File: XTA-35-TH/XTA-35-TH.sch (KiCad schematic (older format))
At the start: 28 parts, among them J1 XTA_Connector, J2 XTA Power, J3 LED, J4 SD0, J5 SD1, J6 DEBUG, SW1 Boot Override, SW2 Reset, U1 74LVC245, U2 74LVC245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

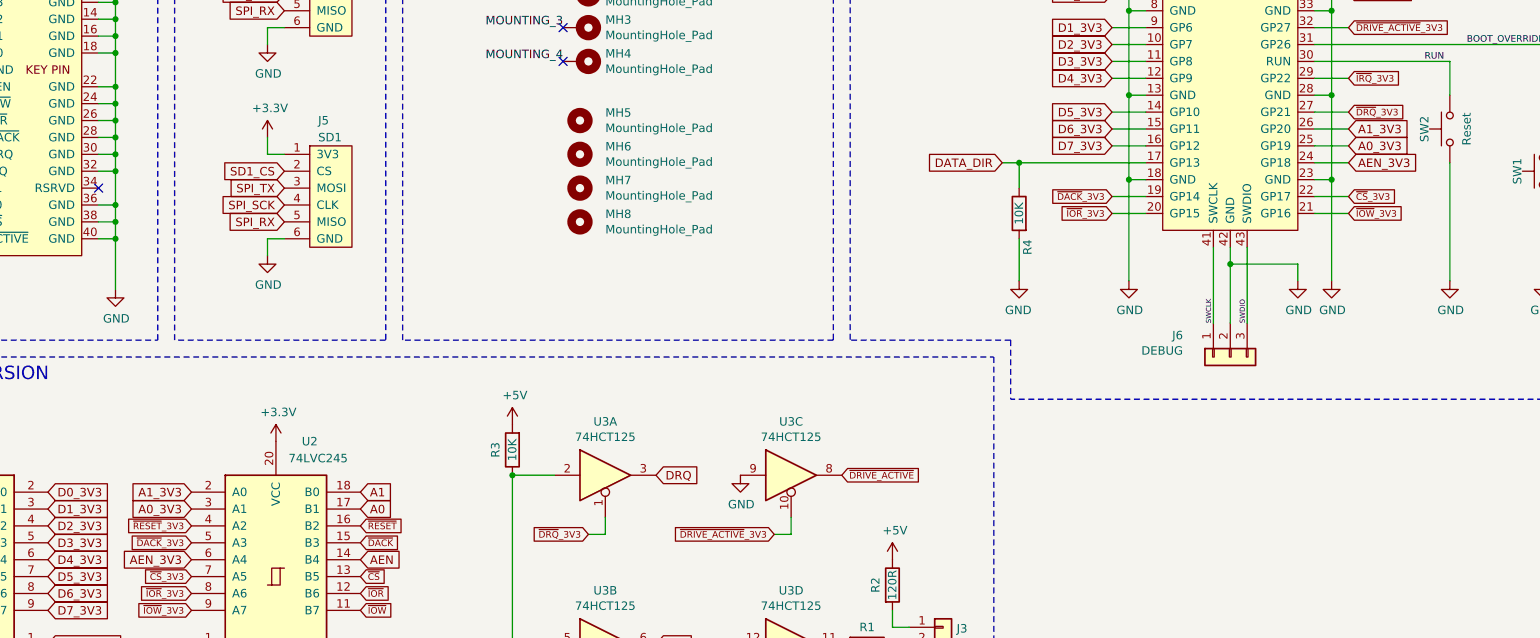
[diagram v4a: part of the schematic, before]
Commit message: Swap A0/A1 pin assignments.
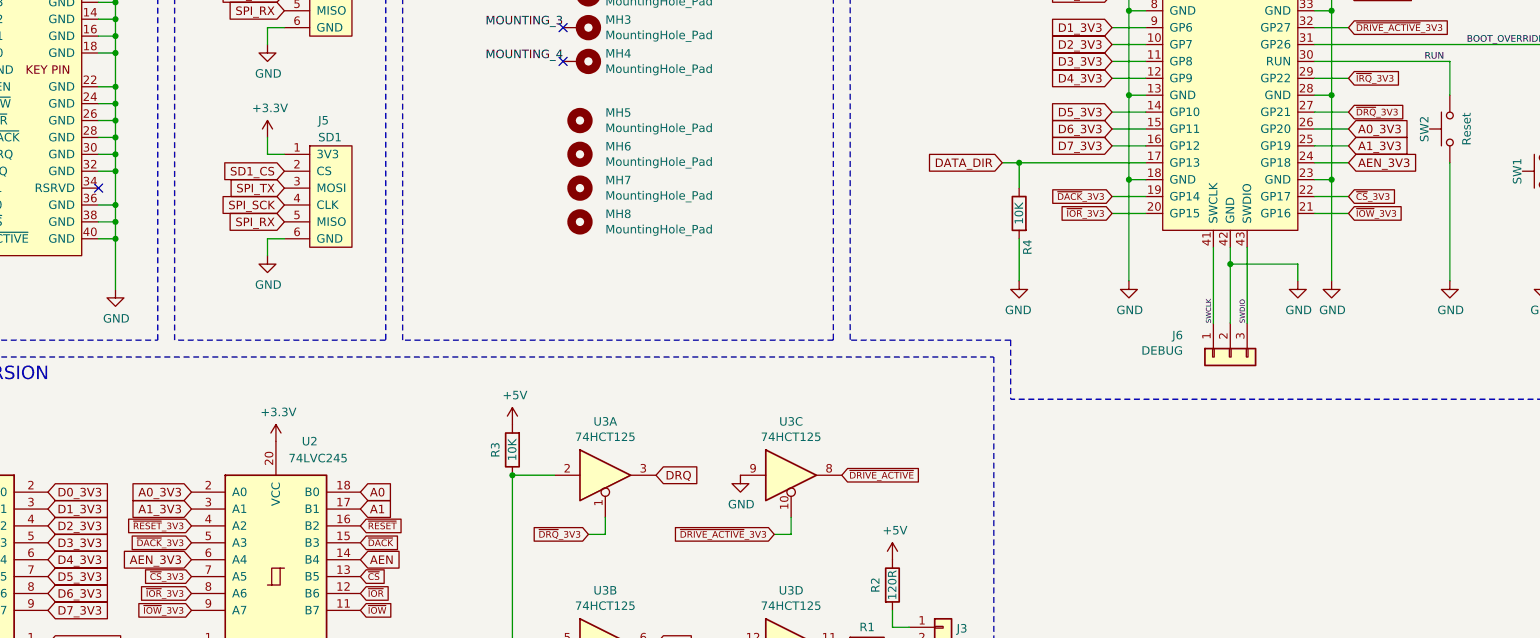
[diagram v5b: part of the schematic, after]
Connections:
- net A0: now also U2.18 (B0); no longer U2.17 (B1)
- net A0_3V3: now also U2.2 (A0), U5.26 (GP20); no longer U2.3 (A1), U5.25 (GP19)
- net A1: now also U2.17 (B1); no longer U2.18 (B0)
- net A1_3V3: now also U2.3 (A1), U5.25 (GP19); no longer U2.2 (A0), U5.26 (GP20)
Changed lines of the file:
@@
 Text GLabel 8150 2450 0    50   Input ~ 0
 D7_3V3
+Text GLabel 9550 2350 2    50   Input ~ 0
+A0_3V3
+Wire Wire Line
+	8150 1950 8350 1950
 Text GLabel 9550 2450 2    50   Input ~ 0
-A0_3V3
-Wire Wire Line
-	8150 1950 8350 1950
-Text GLabel 9550 2350 2    50   Input ~ 0
 A1_3V3
 Wire Wire Line
@@
 Text Label 9350 1250 0    39   ~ 0
 3V3_EN
+Text GLabel 2700 4600 0    50   Input ~ 0
+A1_3V3
 Text GLabel 2700 4500 0    50   Input ~ 0
-A1_3V3
-Text GLabel 2700 4600 0    50   Input ~ 0
 A0_3V3
 Text GLabel 2700 4800 0    39   Input ~ 0
@@
 Text GLabel 2700 4900 0    50   Input ~ 0
 AEN_3V3
-Text GLabel 3700 4500 2    50   Input ~ 0
+Text GLabel 3700 4600 2    50   Input ~ 0
 A1
 Text GLabel 3700 4900 2    50   Input ~ 0
@@
 Wire Wire Line
 	7850 950  8350 950
-Text GLabel 3700 4600 2    50   Input ~ 0
+Text GLabel 3700 4500 2    50   Input ~ 0
 A0
 Wire Wire Line

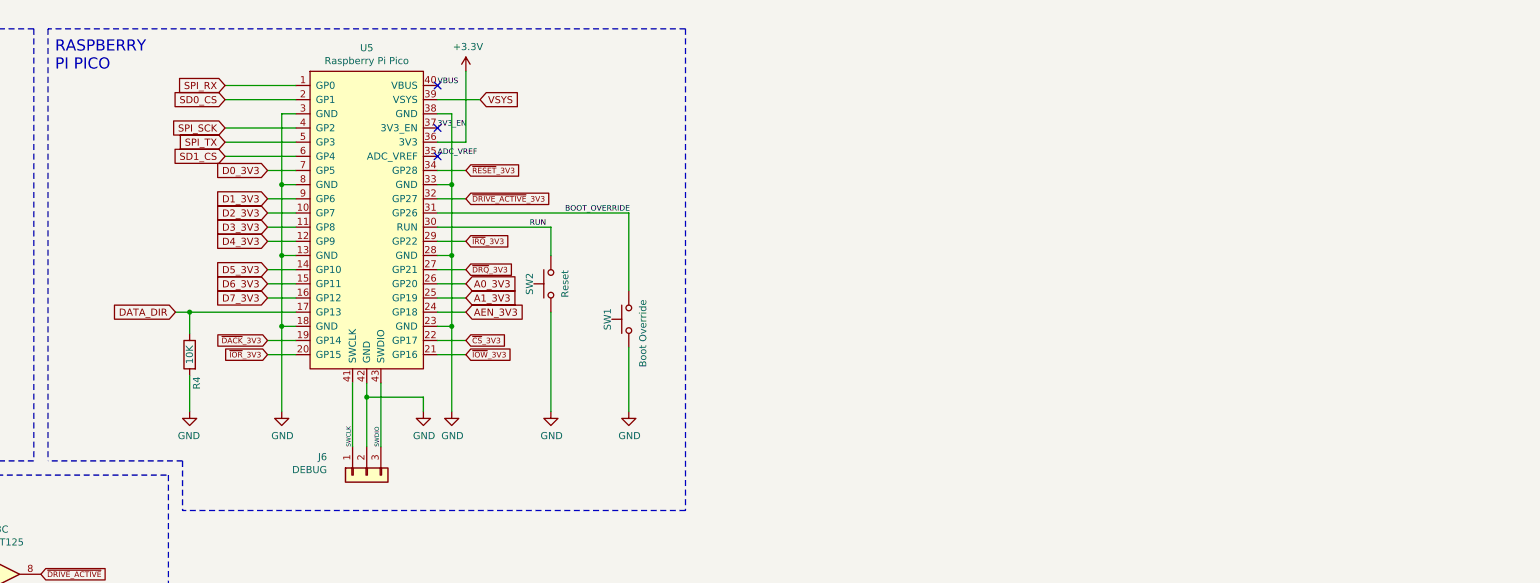
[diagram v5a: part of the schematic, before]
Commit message: Add pullup resistors to ~IRQ and ~DRQ.
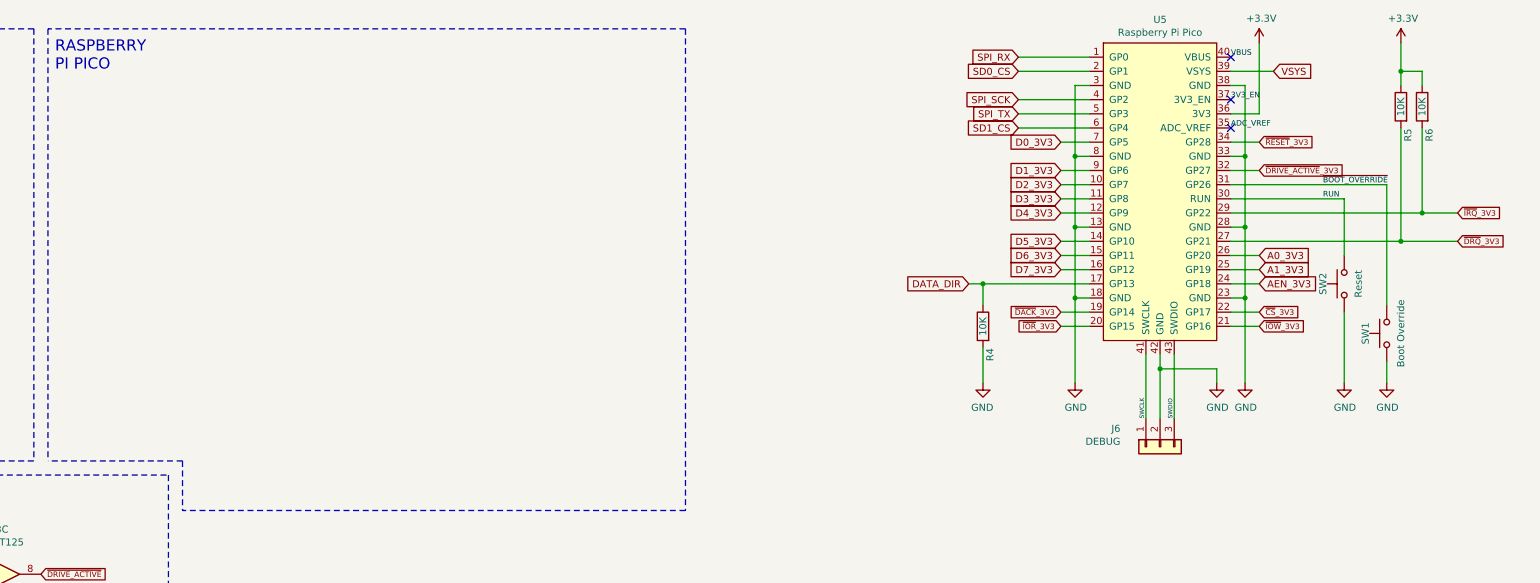
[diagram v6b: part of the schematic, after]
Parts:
- added R5, R6: 10K, Resistor_SMD:R_1206_3216Metric, symbol Device:R
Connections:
- net +3V3: now also R5.1, R6.1
- net ~DRQ~_3V3: now also R5.2
- net ~IRQ~_3V3: now also R6.2
- net BOOT_OVERRIDE renamed ~BOOT_OVERRIDE
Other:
- moved on the sheet: J6, R4, SW1, SW2, U5
